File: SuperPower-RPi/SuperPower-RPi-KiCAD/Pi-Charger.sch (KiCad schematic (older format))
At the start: 16 parts, among them U2 BQ25895RTW

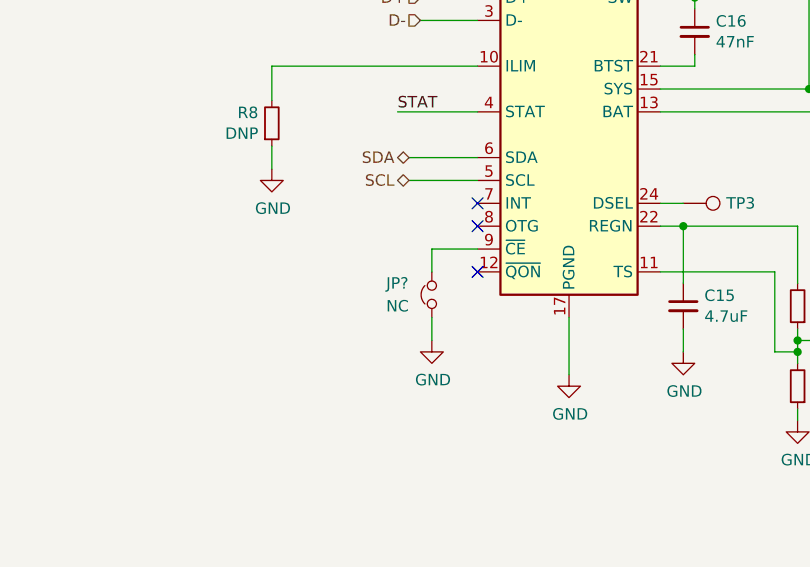
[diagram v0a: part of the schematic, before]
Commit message: Added DotStar to MCU page, and a jumper to Boost converter Enable pin.
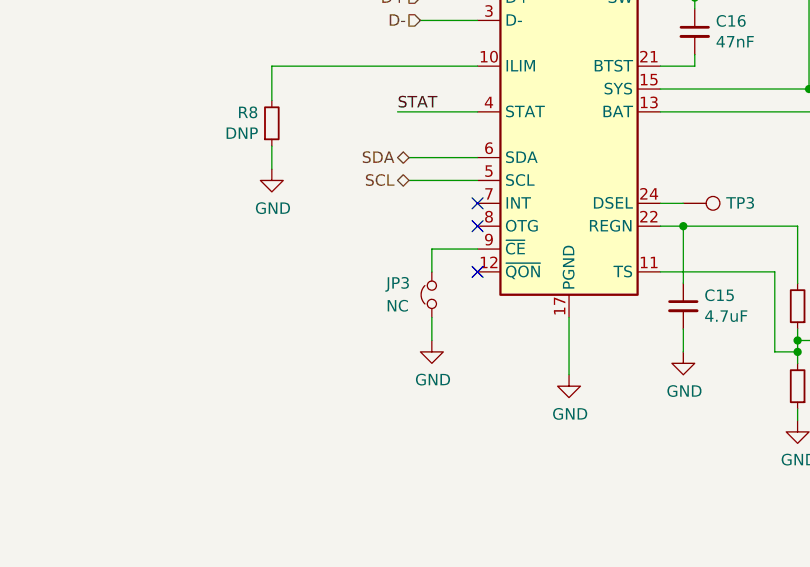
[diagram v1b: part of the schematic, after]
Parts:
- gave numbers to parts that had none: 1
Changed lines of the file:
@@
 	6650 5100 6650 5050
 $Comp
-L Device:Jumper_NC_Small JP?
+L Device:Jumper_NC_Small JP3
 U 1 1 5FBBB98D
 P 5050 4550
-F 0 "JP?" V 5100 4750 50  0000 R CNN
+F 0 "JP3" V 5100 4750 50  0000 R CNN
 F 1 "NC" V 5000 4750 50  0000 R CNN
 F 2 "Jumper:SolderJumper-2_P1.3mm_Bridged_Pad1.0x1.5mm" H 5050 4550 50  0001 C CNN

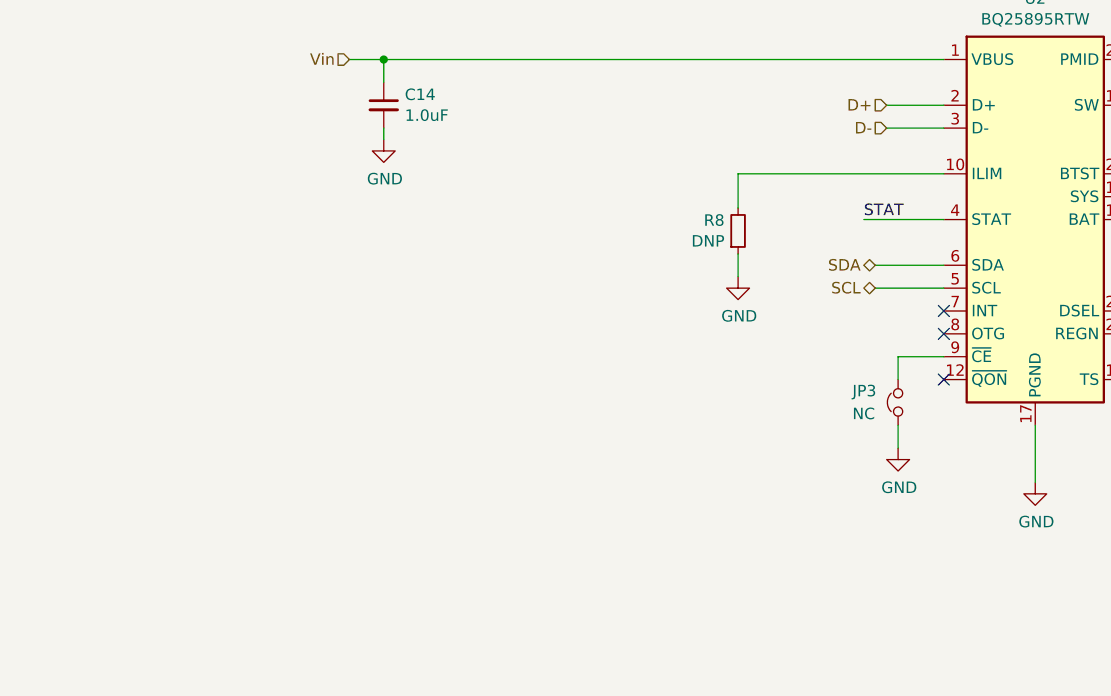
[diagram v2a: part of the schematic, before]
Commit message: Popoulated ILIM Resistor with 220 Ohm part.  Added TPs for other pins.
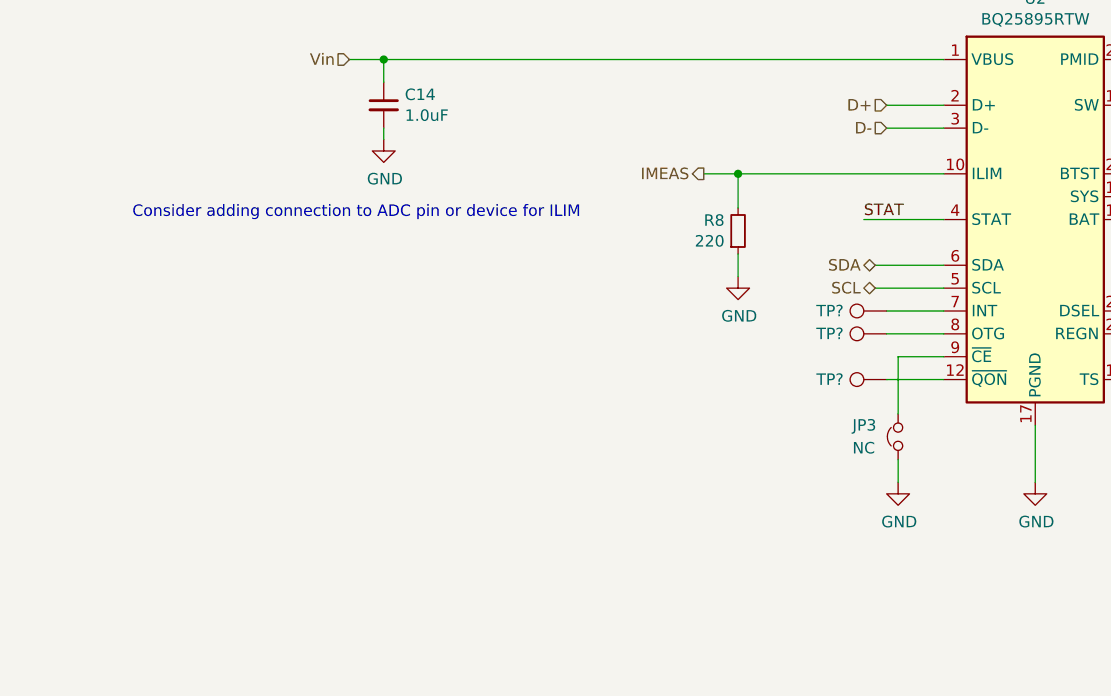
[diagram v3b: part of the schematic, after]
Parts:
- added TP? (x3): DNP, TestPoint:TestPoint_Pad_1.0x1.0mm, symbol Connector:TestPoint
- R8: value DNP -> 220; Digi-Key PN (none) -> 311-220HRCT-ND; Mfg (none) -> Yageo; Mfg PN (none) -> RC0603FR-07220RL
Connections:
- net IMEAS: now reaches R8.2, U2.10 (ILIM)
- net at U2.12 (~QON): now also TP?.1
- net at U2.7 (INT): now also TP?.1
- net at U2.8 (OTG): now also TP?.1
- no-connect marks 3 -> 0
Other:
- note added: "Consider adding connection to ADC pin or device for ILIM"
- moved on the sheet: JP3
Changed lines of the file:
@@
 	1    0    0    -1
 $EndComp
-NoConn ~ 5250 4250
 Wire Wire Line
 	2650 3050 2800 3050
@@
 P 4350 3800
 F 0 "R8" H 4291 3754 50  0000 R CNN
-F 1 "DNP" H 4291 3845 50  0000 R CNN
+F 1 "220" H 4291 3845 50  0000 R CNN
 F 2 "Resistor_SMD:R_0603_1608Metric" H 4350 3800 50  0001 C CNN
 F 3 "~" H 4350 3800 50  0001 C CNN
+F 4 "Yageo" H 4350 3800 50  0001 C CNN "Mfg"
+F 5 "RC0603FR-07220RL" H 4350 3800 50  0001 C CNN "Mfg PN"
+F 6 "311-220HRCT-ND" H 4350 3800 50  0001 C CNN "Digi-Key PN"
 	1    4350 3800
 	1    0    0    1
@@
 L power:GND #PWR013
 U 1 1 5F7917AE
-P 5050 4750
-F 0 "#PWR013" H 5050 4500 50  0001 C CNN
-F 1 "GND" H 5055 4577 50  0000 C CNN
-F 2 "" H 5050 4750 50  0001 C CNN
-F 3 "" H 5050 4750 50  0001 C CNN
-	1    5050 4750
+P 5050 4900
+F 0 "#PWR013" H 5050 4650 50  0001 C CNN
+F 1 "GND" H 5055 4727 50  0000 C CNN
+F 2 "" H 5050 4900 50  0001 C CNN
+F 3 "" H 5050 4900 50  0001 C CNN
+	1    5050 4900
 	1    0    0    -1
 $EndComp
@@
 Wire Wire Line
 	6900 4100 6900 4050
-NoConn ~ 5250 4150
-NoConn ~ 5250 4450
 $Comp
 L power:GND #PWR0108
@@
 L Device:Jumper_NC_Small JP3
 U 1 1 5FBBB98D
-P 5050 4550
-F 0 "JP3" V 5100 4750 50  0000 R CNN
-F 1 "NC" V 5000 4750 50  0000 R CNN
-F 2 "Jumper:SolderJumper-2_P1.3mm_Bridged_Pad1.0x1.5mm" H 5050 4550 50  0001 C CNN
-F 3 "~" H 5050 4550 50  0001 C CNN
-	1    5050 4550
+P 5050 4700
+F 0 "JP3" V 5100 4900 50  0000 R CNN
+F 1 "NC" V 5000 4900 50  0000 R CNN
+F 2 "Jumper:SolderJumper-2_P1.3mm_Bridged_Pad1.0x1.5mm" H 5050 4700 50  0001 C CNN
+F 3 "~" H 5050 4700 50  0001 C CNN
+	1    5050 4700
 	0    -1   -1   0
 $EndComp
 Wire Wire Line
-	5050 4450 5050 4350
-Wire Wire Line
-	5050 4650 5050 4750
+	5050 4800 5050 4900
+Text Notes 1700 3750 0    50   ~ 0
+Consider adding connection to ADC pin or device for ILIM
+Text HLabel 4200 3550 0    50   Output ~ 0
+IMEAS
+Wire Wire Line
+	4200 3550 4350 3550
+Connection ~ 4350 3550
+$Comp
+L Connector:TestPoint TP?
+U 1 1 5FC0654F
+P 5000 4150
+F 0 "TP?" V 5000 4338 50  0000 L CNN
+F 1 "DNP" H 5058 4177 50  0001 L CNN
+F 2 "TestPoint:TestPoint_Pad_1.0x1.0mm" H 5200 4150 50  0001 C CNN
+F 3 "~" H 5200 4150 50  0001 C CNN
+	1    5000 4150
+	0    -1   -1   0
+$EndComp
+$Comp
+L Connector:TestPoint TP?
+U 1 1 5FC06D49
+P 5000 4250
+F 0 "TP?" V 5000 4438 50  0000 L CNN
+F 1 "DNP" H 5058 4277 50  0001 L CNN
+F 2 "TestPoint:TestPoint_Pad_1.0x1.0mm" H 5200 4250 50  0001 C CNN
+F 3 "~" H 5200 4250 50  0001 C CNN
+	1    5000 4250
+	0    -1   -1   0
+$EndComp
+Wire Wire Line
+	5050 4350 5050 4600
+$Comp
+L Connector:TestPoint TP?
+U 1 1 5FC09313
+P 5000 4450
+F 0 "TP?" V 5000 4638 50  0000 L CNN
+F 1 "DNP" H 5058 4477 50  0001 L CNN
+F 2 "TestPoint:TestPoint_Pad_1.0x1.0mm" H 5200 4450 50  0001 C CNN
+F 3 "~" H 5200 4450 50  0001 C CNN
+	1    5000 4450
+	0    -1   -1   0
+$EndComp
+Wire Wire Line
+	5000 4450 5250 4450
+Wire Wire Line
+	5250 4250 5000 4250
+Wire Wire Line
+	5000 4150 5250 4150
 $EndSCHEMATC

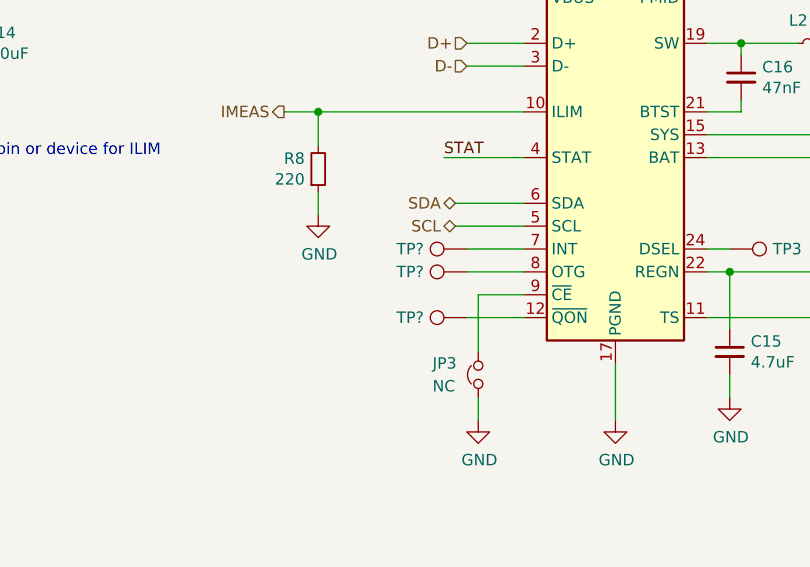
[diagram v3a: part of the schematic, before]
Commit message: Made connections between Pi and MCU, and cleared up some ERC errors.
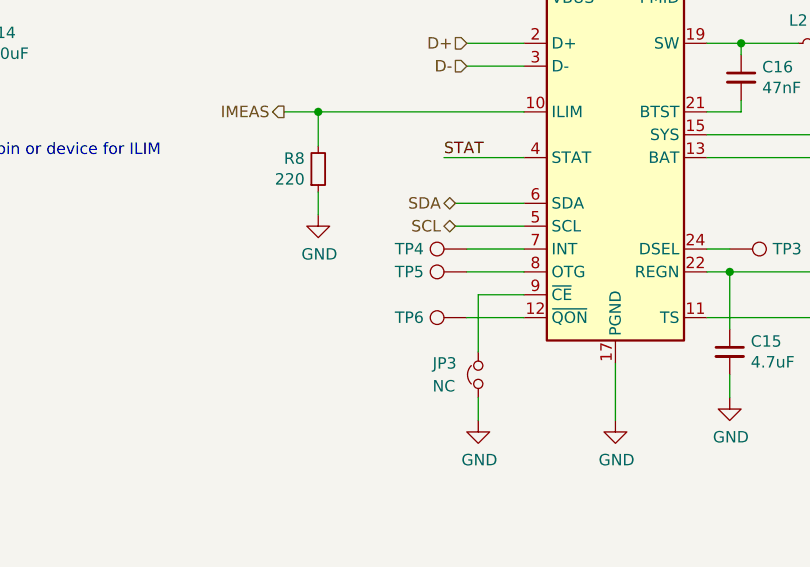
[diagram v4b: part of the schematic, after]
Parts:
- gave numbers to parts that had none: 3
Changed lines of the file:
@@
 Connection ~ 4350 3550
 $Comp
-L Connector:TestPoint TP?
+L Connector:TestPoint TP4
 U 1 1 5FC0654F
 P 5000 4150
-F 0 "TP?" V 5000 4338 50  0000 L CNN
+F 0 "TP4" V 5000 4338 50  0000 L CNN
 F 1 "DNP" H 5058 4177 50  0001 L CNN
 F 2 "TestPoint:TestPoint_Pad_1.0x1.0mm" H 5200 4150 50  0001 C CNN
@@
 $EndComp
 $Comp
-L Connector:TestPoint TP?
+L Connector:TestPoint TP5
 U 1 1 5FC06D49
 P 5000 4250
-F 0 "TP?" V 5000 4438 50  0000 L CNN
+F 0 "TP5" V 5000 4438 50  0000 L CNN
 F 1 "DNP" H 5058 4277 50  0001 L CNN
 F 2 "TestPoint:TestPoint_Pad_1.0x1.0mm" H 5200 4250 50  0001 C CNN
@@
 	5050 4350 5050 4600
 $Comp
-L Connector:TestPoint TP?
+L Connector:TestPoint TP6
 U 1 1 5FC09313
 P 5000 4450
-F 0 "TP?" V 5000 4638 50  0000 L CNN
+F 0 "TP6" V 5000 4638 50  0000 L CNN
 F 1 "DNP" H 5058 4477 50  0001 L CNN
 F 2 "TestPoint:TestPoint_Pad_1.0x1.0mm" H 5200 4450 50  0001 C CNN

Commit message: PCB Updates.
Added new components, and did some arranging.
Updates TPS61088 and bq25895 footprints to use 0.3mm vias.  PCBWay's minimum via size is 0.3mm.
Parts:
- U2: footprint Package_DFN_QFN:Texas_S-PWQFN-N24_EP2.7x2.7mm_ThermalVias -> SuperPower-RPi-KiCAD:Texas_S-PWQFN-N24_EP2.7x2.7mm_ThermalVias
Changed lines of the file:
@@
 F 0 "U2" H 5650 4717 50  0000 C CNN
 F 1 "BQ25895RTW" H 5650 4626 50  0000 C CNN
-F 2 "Package_DFN_QFN:Texas_S-PWQFN-N24_EP2.7x2.7mm_ThermalVias" H 5550 4750 50  0001 C CNN
+F 2 "SuperPower-RPi-KiCAD:Texas_S-PWQFN-N24_EP2.7x2.7mm_ThermalVias" H 5550 4750 50  0001 C CNN
 F 3 "http://www.ti.com/lit/ds/symlink/bq25895.pdf" H 5450 4550 50  0001 C CNN
 F 4 "296-44345-1-ND" H 5650 3750 50  0001 C CNN "Digi-Key PN"

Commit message: Changed some passives to 0402 and added some part meta-data.
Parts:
- C16: footprint Capacitor_SMD:C_0603_1608Metric -> Capacitor_SMD:C_0402_1005Metric; Digi-Key PN (none) -> 490-3254-1-ND; Mfg Yageo -> Murata; Mfg PN CC0603KRX7R9BB473 -> GRM155R71E473KA88D
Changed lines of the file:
@@
 F 0 "C16" H 6292 3446 50  0000 L CNN
 F 1 "47nF" H 6292 3355 50  0000 L CNN
-F 2 "Capacitor_SMD:C_0603_1608Metric" H 6200 3400 50  0001 C CNN
-F 3 "~" H 6200 3400 50  0001 C CNN
-F 4 "Yageo" H 6200 3400 50  0001 C CNN "Mfg"
-F 5 "CC0603KRX7R9BB473" H 6200 3400 50  0001 C CNN "Mfg PN"
+F 2 "Capacitor_SMD:C_0402_1005Metric" H 6200 3400 50  0001 C CNN
+F 3 "https://search.murata.co.jp/Ceramy/image/img/A01X/G101/ENG/GRM155R71E473KA88-01.pdf" H 6200 3400 50  0001 C CNN
+F 4 "Murata" H 6200 3400 50  0001 C CNN "Mfg"
+F 5 "GRM155R71E473KA88D" H 6200 3400 50  0001 C CNN "Mfg PN"
+F 6 "490-3254-1-ND" H 6200 3400 50  0001 C CNN "Digi-Key PN"
 	1    6200 3400
 	1    0    0    -1

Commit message: Updated meta-data.
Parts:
- D2, JP3, R7, TP3, TP4, TP5, TP6: Mfg (none) -> DNP
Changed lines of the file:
@@
 F 2 "LED_SMD:LED_0603_1608Metric" H 2750 2000 50  0001 C CNN
 F 3 "~" H 2750 2000 50  0001 C CNN
+F 4 "DNP" H 2750 2000 50  0001 C CNN "Mfg"
 	1    2750 2000
 	0    -1   -1   0
@@
 F 2 "Resistor_SMD:R_0603_1608Metric" H 2750 1700 50  0001 C CNN
 F 3 "~" H 2750 1700 50  0001 C CNN
+F 4 "DNP" H 2750 1700 50  0001 C CNN "Mfg"
 	1    2750 1700
 	1    0    0    1
@@
 F 2 "TestPoint:TestPoint_Keystone_5000-5004_Miniature" H 6350 4150 50  0001 C CNN
 F 3 "~" H 6350 4150 50  0001 C CNN
+F 4 "DNP" H 6150 4150 50  0001 C CNN "Mfg"
 	1    6150 4150
 	0    1    1    0
@@
 F 2 "Jumper:SolderJumper-2_P1.3mm_Bridged_Pad1.0x1.5mm" H 5050 4700 50  0001 C CNN
 F 3 "~" H 5050 4700 50  0001 C CNN
+F 4 "DNP" H 5050 4700 50  0001 C CNN "Mfg"
 	1    5050 4700
 	0    -1   -1   0
@@
 F 2 "TestPoint:TestPoint_Pad_1.0x1.0mm" H 5200 4150 50  0001 C CNN
 F 3 "~" H 5200 4150 50  0001 C CNN
+F 4 "DNP" H 5000 4150 50  0001 C CNN "Mfg"
 	1    5000 4150
 	0    -1   -1   0
@@
 F 2 "TestPoint:TestPoint_Pad_1.0x1.0mm" H 5200 4250 50  0001 C CNN
 F 3 "~" H 5200 4250 50  0001 C CNN
+F 4 "DNP" H 5000 4250 50  0001 C CNN "Mfg"
 	1    5000 4250
 	0    -1   -1   0
@@
 F 2 "TestPoint:TestPoint_Pad_1.0x1.0mm" H 5200 4450 50  0001 C CNN
 F 3 "~" H 5200 4450 50  0001 C CNN
+F 4 "DNP" H 5000 4450 50  0001 C CNN "Mfg"
 	1    5000 4450
 	0    -1   -1   0

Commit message: Updated 1uF caps to 0402 package.
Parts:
- C14, C18, C26: footprint Capacitor_SMD:C_0603_1608Metric -> Capacitor_SMD:C_0402_1005Metric; Digi-Key PN 1276-1184-1-ND -> 490-10017-1-ND; Mfg Samsung -> Murata Electronics; Mfg PN CL10B105KA8NNNC -> GRM155R61E105KA12D
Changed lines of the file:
@@
 F 0 "C14" H 2892 3296 50  0000 L CNN
 F 1 "1.0uF" H 2892 3205 50  0000 L CNN
-F 2 "Capacitor_SMD:C_0603_1608Metric" H 2800 3250 50  0001 C CNN
+F 2 "Capacitor_SMD:C_0402_1005Metric" H 2800 3250 50  0001 C CNN
 F 3 "~" H 2800 3250 50  0001 C CNN
-F 4 "Samsung" H 2800 3250 50  0001 C CNN "Mfg"
-F 5 "CL10B105KA8NNNC" H 2800 3250 50  0001 C CNN "Mfg PN"
-F 6 "1276-1184-1-ND" H 2800 3250 50  0001 C CNN "Digi-Key PN"
+F 4 "Murata Electronics" H 2800 3250 50  0001 C CNN "Mfg"
+F 5 "GRM155R61E105KA12D" H 2800 3250 50  0001 C CNN "Mfg PN"
+F 6 "490-10017-1-ND" H 2800 3250 50  0001 C CNN "Digi-Key PN"
 	1    2800 3250
 	1    0    0    -1
@@
 F 0 "C18" H 7542 3246 50  0000 L CNN
 F 1 "1.0uF" H 7542 3155 50  0000 L CNN
-F 2 "Capacitor_SMD:C_0603_1608Metric" H 7450 3200 50  0001 C CNN
+F 2 "Capacitor_SMD:C_0402_1005Metric" H 7450 3200 50  0001 C CNN
 F 3 "~" H 7450 3200 50  0001 C CNN
-F 4 "Samsung" H 7450 3200 50  0001 C CNN "Mfg"
-F 5 "CL10B105KA8NNNC" H 7450 3200 50  0001 C CNN "Mfg PN"
-F 6 "1276-1184-1-ND" H 7450 3200 50  0001 C CNN "Digi-Key PN"
+F 4 "Murata Electronics" H 7450 3200 50  0001 C CNN "Mfg"
+F 5 "GRM155R61E105KA12D" H 7450 3200 50  0001 C CNN "Mfg PN"
+F 6 "490-10017-1-ND" H 7450 3200 50  0001 C CNN "Digi-Key PN"
 	1    7450 3200
 	1    0    0    -1
@@
 F 0 "C26" H 8192 3846 50  0000 L CNN
 F 1 "1.0uF" H 8192 3755 50  0000 L CNN
-F 2 "Capacitor_SMD:C_0603_1608Metric" H 8100 3800 50  0001 C CNN
+F 2 "Capacitor_SMD:C_0402_1005Metric" H 8100 3800 50  0001 C CNN
 F 3 "~" H 8100 3800 50  0001 C CNN
-F 4 "Samsung" H 8100 3800 50  0001 C CNN "Mfg"
-F 5 "CL10B105KA8NNNC" H 8100 3800 50  0001 C CNN "Mfg PN"
-F 6 "1276-1184-1-ND" H 8100 3800 50  0001 C CNN "Digi-Key PN"
+F 4 "Murata Electronics" H 8100 3800 50  0001 C CNN "Mfg"
+F 5 "GRM155R61E105KA12D" H 8100 3800 50  0001 C CNN "Mfg PN"
+F 6 "490-10017-1-ND" H 8100 3800 50  0001 C CNN "Digi-Key PN"
 	1    8100 3800
 	1    0    0    -1
